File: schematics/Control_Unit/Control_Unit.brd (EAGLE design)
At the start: 58.4 x 86.3 mm, 191 parts, among them IC1 74HC174N, IC10 74HC74N, IC100 74HCT32N, IC101 74HCT08N, IC102 74HC151N, IC103 74HC373N, IC104 74HCT08N, IC105 74HC151N, IC106 74HC151N, IC107 74HCT04N, IC108 74HCT32N, IC109 74HCT08N, IC11 74HC74N, IC110 74HCT32N, IC111 74HC151N, IC112 74HCT32N, IC113 74HC151N, IC114 74HC151N, IC115 74HC151N, IC116 74HC373N, IC117 74HC74N, IC118 74HCT08N, IC119 74HCT08N, IC12 74AC08N, IC120 74HCT04N, IC121 74HCT04N, IC122 74HCT04N, IC123 74HCT04N, IC124 74HCT32N, IC125 74HCT08N, IC126 74AC157N, IC127 74HCT08N, IC128 74AC08N, IC129 74AC08N, IC13 74AC08N, IC130 74HCT04N, IC131 74HCT04N, IC132 74HCT04N, IC133 74HCT04N, IC134 74HCT08N, IC135 74HCT08N, IC136 74HCT08N, IC137 74HCT08N, IC138 74HCT04N, IC139 74HCT08N, IC14 74HC74N, IC140 74HCT08N, IC141 74HCT32N, IC142 74HCT32N, IC143 74HCT32N, IC144 74HCT32N, IC145 74HCT32N, IC146 74HCT32N, IC147 74HCT32N, IC148 74HCT32N, IC15 74HC74N, IC16 74AC08N, IC164 74HC174N, IC165 74HC174N, IC166 74HC174N, IC167 74HC174N, IC168 74HCT32N, IC169 74HCT32N, IC17 74HCT32N, IC172 74HCT32N, IC173 74HCT32N, IC175 74HC193N, IC176 74HC193N, IC177 74HC193N, IC178 74HC193N, IC179 74HC193N, IC18 74AC08N, IC180 74HC193N, IC181 74HC193N, IC182 74HC193N, IC19 74AC08N, IC190 74HCT32N, IC191 74HCT32N, IC2 74HC174N, IC20 74AC08N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

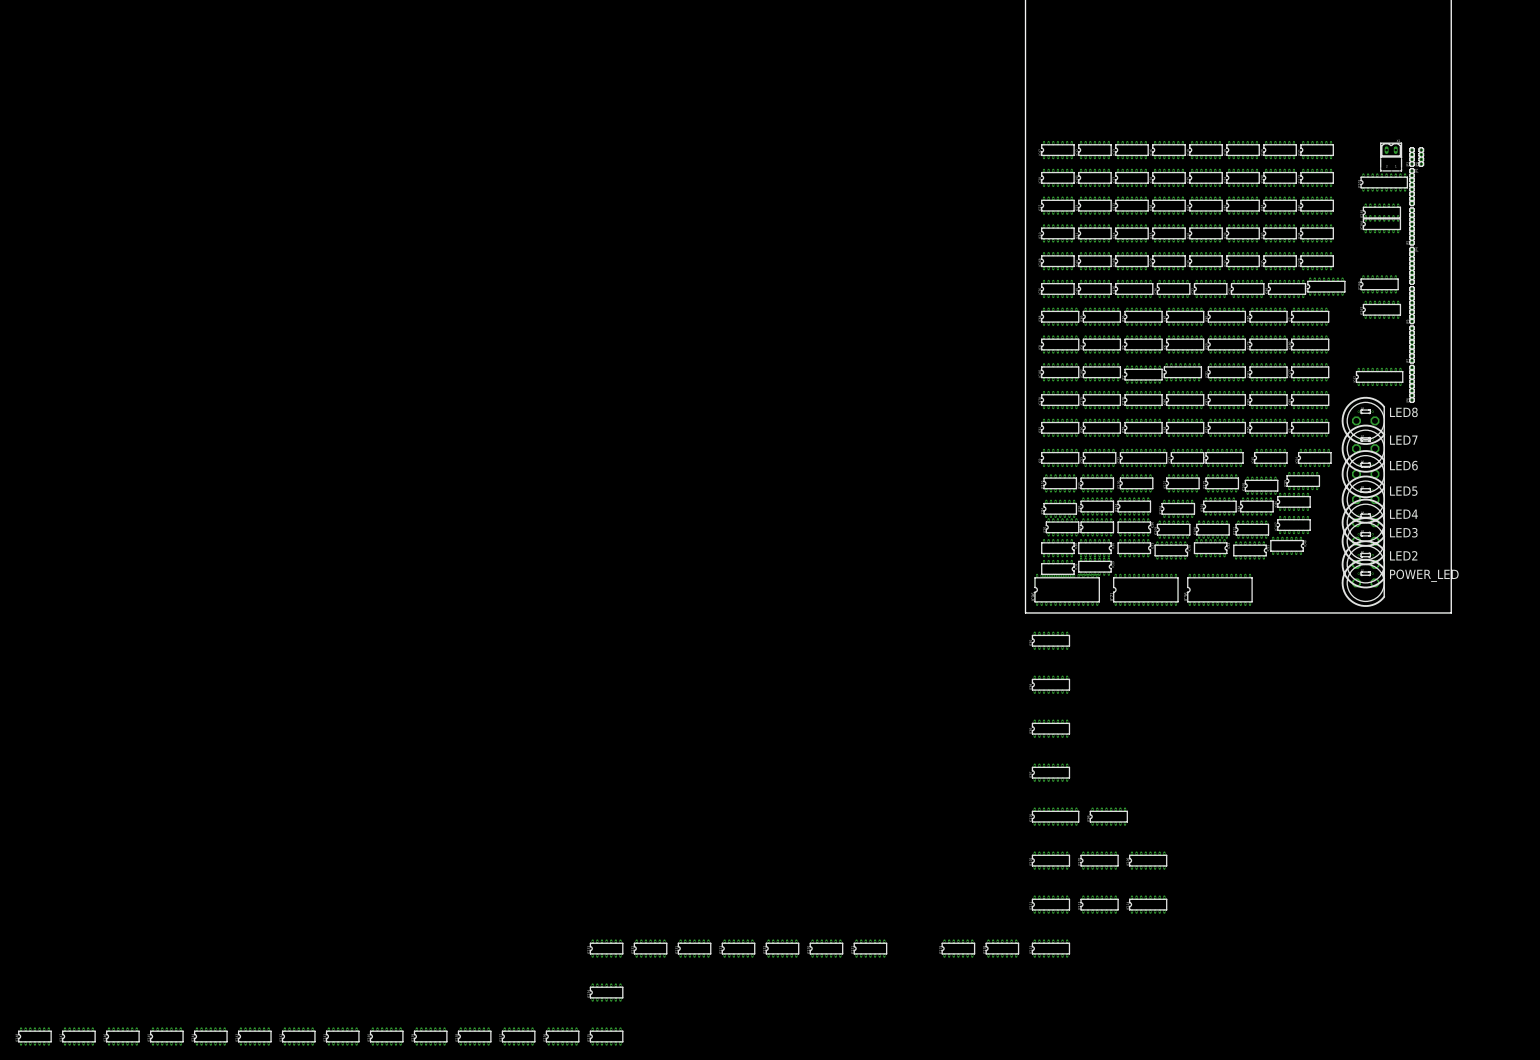
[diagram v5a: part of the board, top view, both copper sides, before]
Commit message: finish ringcounter
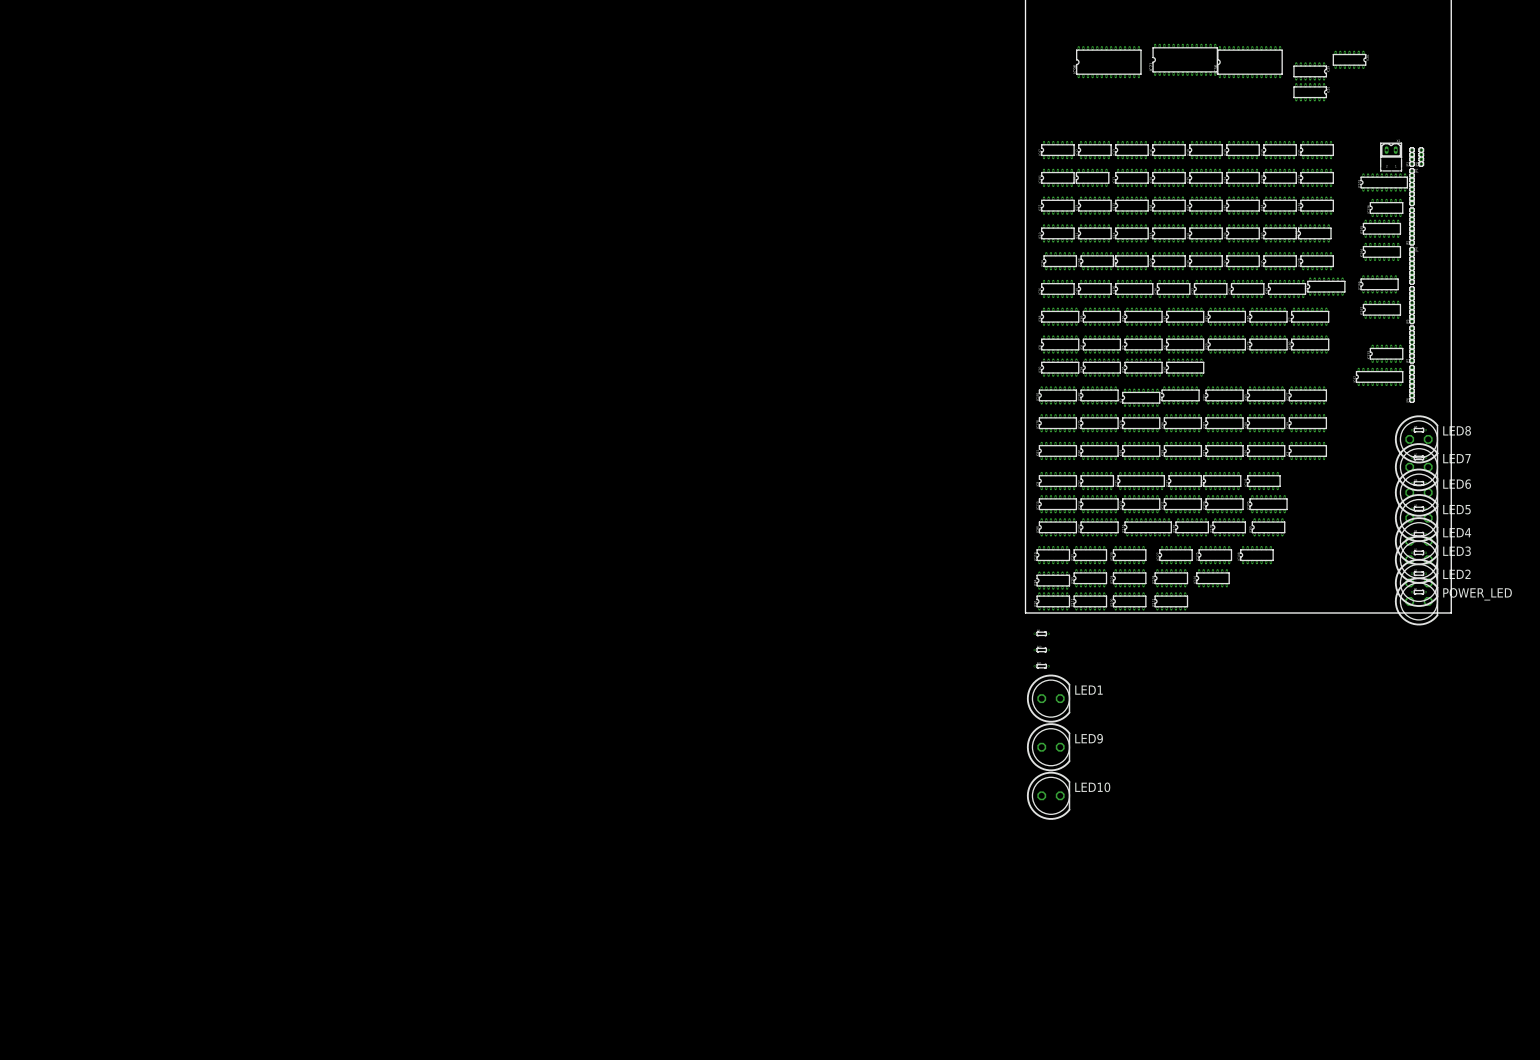
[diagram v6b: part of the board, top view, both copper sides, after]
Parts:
- removed IC118, IC119, IC137, IC139, IC140, IC53, IC64, IC70, IC73, IC90: 74HCT08N, 74xx-eu:DIL14
- removed IC120, IC121, IC122, IC123, IC131, IC132, IC138, IC44, IC45, IC54: 74HCT04N, 74xx-eu:DIL14
- removed IC142, IC143, IC144, IC145, IC146, IC147, IC148, IC31, IC40, IC48, IC85, IC99: 74HCT32N, 74xx-eu:DIL14
- added LED1, LED10, LED9: (no value), led:LED5MM
- added R10, R11, R9: (no value), resistor:0204/7
- moved IC136 160.3 mm to (49.8, 55.6)
- moved IC141 147.6 mm to (33.0, 18.1)
- moved IC135 146.9 mm to (40.0, 52.1)
- moved IC134 145.4 mm to (40.3, 55.9)
- moved IC133 134.6 mm to (49.8, 35.6)
- moved IC81 75.5 mm to (44.8, 75.9)
- moved IC29 74.1 mm to (39.4, 74.3)
- moved IC71 72.9 mm to (22.2, 75.9)
- moved IC96 72.6 mm to (11.7, 75.6)
- moved IC36 72.5 mm to (31.1, 75.6)
- moved IC51 63.4 mm to (39.4, 71.4)
- moved IC115 61.0 mm to (4.76, 14.9)
- moved IC97 58.5 mm to (22.2, 33.7)
- moved IC111 57.8 mm to (21.9, 14.9)
- moved IC114 55.3 mm to (10.5, 14.9)
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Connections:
- net NOT_USED05 renamed NOT_USED5
- net SP_DATA_OUT_15 renamed SP_DATA_OUT_UNUSED
- removed net CARRY_SET_JMPC: IC78.9
- removed net CLR_SP: IC175.14, IC176.14, IC177.14, IC178.14
- removed net CYCL_10: IC10.2, IC117.9
- removed net CYCL_5: IC14.12, IC14.5
- removed net CYCL_6: IC14.9, IC15.2
- removed net CYCL_7: IC15.12, IC15.5
- removed net CYCL_8: IC117.2, IC15.9
- removed net CYCL_9: IC117.12, IC117.5
- removed net DATA10: IC116.6
- removed net DATA11: IC116.9
- removed net DATA12: IC116.12
- removed net DATA13: IC116.15
- removed net DATA14: IC116.16
- removed net DATA15: IC116.19
- removed net DATA8: IC116.2
- removed net DATA9: IC116.5
- removed net RING_CNTR_CLR: IC10.13, IC10.4, IC11.1, IC11.13, IC117.1, IC117.13, IC14.1, IC14.13, IC15.1, IC15.13
- removed net STATE_5: IC101.1, IC127.4
- removed net WRITE_REG_TO_DBUS_JMP_O: IC33.1
- new net !RING_CNTR_RESET: IC10.13, IC10.4, IC11.1, IC11.13, IC117.1, IC117.13, IC14.1, IC14.13, IC15.1, IC15.13, IC43.2
- new net N$225: LED10.A
- new net PC_COUNT_UP_FETCH2: IC124.2, IC14.12, IC14.5
- new net RING_CNTR_RESET: IC43.1
- new net STATE_0: IC101.9, IC14.9, IC15.2, IC23.1, IC23.12, IC24.12, IC27.9, IC28.1, IC38.9, IC51.4, IC74.1, IC74.9, IC78.12, IC81.12
- net ALU_CARRY_OUT: now also IC78.9
- net DATA0: now also IC116.2
- net DATA1: now also IC116.5
- net DATA2: now also IC116.6
- net DATA3: now also IC116.9
- net DATA4: now also IC116.12
- net DATA5: now also IC116.15
- net DATA6: now also IC116.16
- net DATA7: now also IC116.19
- net DATA_BUS_ENABLE_LATCH: now also IC109.3; no longer IC118.11
- net FILL_LR_H_SAVE_LR: now also IC29.9, IC81.3, IC84.12; no longer IC146.4, IC85.1, IC90.6
- net FILL_LR_L_SAVE_LR: now also IC81.8, IC84.9; no longer IC145.4, IC73.3
- net FILL_PC_H_RET: now also IC29.12, IC51.11, IC80.10; no longer IC147.5, IC48.1, IC70.6
- net FILL_PC_L_JMP_O: now also IC84.1; no longer IC148.4
- net FILL_PC_L_RET: now also IC29.4, IC84.2; no longer IC148.5, IC31.1
- net FSDFAFSDFSFDDDDDDDDDDDDDDDDDDDDDDDDDDDDDDDD1: now also IC136.6; no longer IC137.3
- net GND: now also IC102.12, IC102.13, IC102.14, IC102.15, IC105.12, IC105.13, IC105.14, IC105.15, IC106.12, IC106.13, IC106.14, IC106.15, IC111.12, IC111.13, IC111.14, IC111.15, IC113.12, IC113.13, IC113.14, IC113.15, IC114.12, IC114.13, IC114.14, IC114.15, IC115.12, IC115.13, IC115.14, IC115.15, IC98.12, IC98.13, IC98.14, IC98.15, R10.1, R11.1, R9.1; no longer IC1.1, IC118.7, IC119.7, IC120.7, IC121.7, IC122.7, IC123.7, IC131.7, IC132.7, IC137.7, IC138.7, IC139.7, IC140.7, IC142.7, IC143.7, IC144.7, IC145.7, IC146.7, IC147.7, IC148.7, IC179.14, IC180.14, IC181.14, IC182.14, IC2.1, IC2.11, IC2.13, IC2.14, IC2.6, IC31.7, IC4.1, IC40.7, IC44.7, IC45.7, IC48.7, IC5.1, IC5.11, IC5.13, IC5.14, IC5.6, IC50.1, IC50.11, IC50.13, IC50.14, IC50.6, IC53.7, IC54.7, IC6.1, IC62.1, IC64.7, IC65.1, IC65.11, IC65.13, IC65.14, IC65.6, IC66.1, IC67.1, IC67.11, IC67.13, IC67.14, IC67.6, IC68.1, IC69.1, IC69.11, IC69.13, IC69.14, IC69.6, IC7.1, IC70.7, IC73.7, IC8.1, IC8.11, IC8.13, IC8.14, IC8.6, IC82.14, IC83.14, IC85.7, IC90.7, IC92.1, IC94.1, IC94.11, IC94.13, IC94.14, IC94.6, IC95.1, IC97.1, IC97.11, IC97.13, IC97.14, IC97.6, IC99.7
- net INPUT_REG0: now also IC28.4; no longer IC64.9
- net IR_DATA_OUT_7: now also IC125.10; no longer IC125.9
- net LATCH_ALU_INPUT_B_JMP_O: now also IC110.9, IC17.9; no longer IC40.1, IC99.4
- net LATCH_ALU_INPUT_B_PTR_ADD: now also IC110.10; no longer IC99.5
- net LR_H_LOAD_INPUT: now also IC133.13, IC84.11; no longer IC123.3, IC146.6
- net LR_H_LOAD_INPUT_TABLE_1: now also IC84.13; no longer IC146.5
- net LR_L_LOAD_INPUT: now also IC133.11, IC84.8; no longer IC122.3, IC145.6
- net LR_L_LOAD_INPUT_TABLE_1: now also IC84.10; no longer IC145.5
- net N$100: now also IC124.3, IC133.1; no longer IC54.9, IC99.11
- net N$101: now also LED9.K, R10.2; no longer IC110.10
- net N$109: now also IC17.10; no longer IC40.2
- net N$112: now also IC81.11; no longer IC109.3
- net N$115: now also LED1.K, R9.2; no longer IC110.8, IC77.1, IC79.1
- net N$141: now also IC108.11; no longer IC99.3
- net N$142: now also IC108.12; no longer IC99.1
- net N$144: now also IC108.3; no longer IC99.8
- net N$145: now also IC108.2; no longer IC99.10
- net N$152: now also IC110.8; no longer IC99.6
- net N$163: now also IC84.3; no longer IC148.6
- net N$166: now also IC125.9; no longer IC125.10
- net N$167: now also IC133.12; no longer IC123.4
- net N$168: now also LED1.A; no longer IC99.13
- net N$18: now also IC136.5, IC136.9; no longer IC137.2, IC140.1
- net N$194: now also IC81.10, IC81.13, IC81.2; no longer IC109.2, IC73.2, IC90.5
- net N$195: now also LED9.A; no longer IC80.13, IC91.6
- net N$219: now also IC51.10, IC51.13, IC51.5; no longer IC109.5, IC53.5, IC70.5
- net N$22: now also IC28.6; no longer IC64.8
- net N$221: now also IC43.4; no longer IC44.10
- net N$222: now also IC43.6; no longer IC44.12
- net N$223: now also IC29.5, IC51.6; no longer IC109.6, IC31.2
- net N$224: now also IC136.12; no longer IC139.1
- net N$226: now also IC29.13, IC51.8; no longer IC48.2, IC53.6
- net N$233: now also IC29.10; no longer IC85.2
- net N$234: now also IC133.10; no longer IC122.4
- net N$235: now also IC136.11; no longer IC139.3
- net N$239: now also IC136.8; no longer IC140.3
- net N$247: now also IC136.10, IC136.13, IC43.8; no longer IC138.10, IC139.2, IC140.2
- net N$248: now also IC141.9; no longer IC143.1
- net N$249: now also IC141.10, IC141.11; no longer IC142.3, IC143.2
- net N$250: now also IC141.5, IC141.8; no longer IC143.3, IC144.2
- net N$252: now also IC141.6; no longer IC144.3
- net N$266: now also IC109.2, IC109.5; no longer IC118.13, IC119.13
- net N$267: now also IC107.5, IC109.6; no longer IC119.11, IC121.9
- net N$268: now also IC107.12, IC109.1; no longer IC118.12, IC120.8
- net N$269: now also IC107.6; no longer IC121.8
- net N$70: now also IC107.3; no longer IC45.13
- net N$72: now also IC133.6; no longer IC131.6
- net N$73: now also IC133.4; no longer IC132.6
- net N$90: now also IC141.4; no longer IC144.1
- net N$94: now also LED10.K, R11.2; no longer IC164.1, IC165.1, IC165.11, IC165.13, IC165.14, IC165.6, IC166.1, IC167.1, IC167.11, IC167.13, IC167.14, IC167.6
- net N$99: now also IC107.4; no longer IC45.12
- net OPCODE_4: now also IC43.3; no longer IC44.11
- net OPCODE_5: now also IC43.5; no longer IC44.13
- net OPCODE_7: now also IC136.4, IC43.9; no longer IC137.1, IC138.11
- net OUTPUT_REG0_JMP: now also IC28.5; no longer IC64.10
- net PC_COUNT_UP: now also IC133.2; no longer IC54.8
- net PC_COUNT_UP_FETCH1: now also IC124.1, IC80.13, IC91.6; no longer IC99.12
- net PC_HIGH_LOAD_INPUT: now also IC133.3, IC80.8; no longer IC132.5, IC147.6
- net PC_HIGH_LOAD_INPUT_JMP: now also IC80.9; no longer IC147.4
- net PC_H_COUNT_DOWN_JMP_O: now also IC108.1; no longer IC99.9
- net PC_H_COUNT_UP_JMP_O: now also IC108.13; no longer IC99.2
- net PTR_L_LOAD_INPUT: now also IC133.5; no longer IC131.5
- net REGISTER_OUTPUT_SEL_3: now also IC107.13, IC109.4; no longer IC119.12, IC120.9
- net STATE_1: now also IC104.12, IC15.12, IC15.5, IC23.4, IC24.1, IC26.1, IC27.1, IC27.12, IC38.1, IC51.1, IC74.12, IC74.4, IC75.1, IC81.9; no longer IC101.9, IC109.1, IC109.4, IC23.1, IC23.12, IC24.12, IC27.9, IC28.1, IC38.9, IC74.1, IC74.9, IC78.12
- net STATE_2: now also IC104.1, IC117.2, IC15.9, IC23.9, IC24.4, IC26.4, IC27.4, IC28.9, IC38.4, IC51.9, IC75.4, IC81.4; no longer IC104.12, IC23.4, IC24.1, IC26.1, IC27.1, IC27.12, IC38.1, IC51.1, IC73.1, IC74.12, IC74.4, IC75.1
- net STATE_3: now also IC104.9, IC117.12, IC117.5, IC24.9, IC26.9, IC28.12, IC38.12, IC51.12, IC75.12, IC81.1; no longer IC104.1, IC23.9, IC24.4, IC26.4, IC27.4, IC28.9, IC38.4, IC53.4, IC75.4, IC81.4
- net STATE_4: now also IC10.2, IC101.1, IC117.9, IC127.4; no longer IC104.9, IC24.9, IC26.9, IC28.12, IC38.12, IC70.4, IC75.12, IC90.4
- net VCC: now also IC1.1, IC10.1, IC10.10, IC11.10, IC11.4, IC117.10, IC117.4, IC14.10, IC14.4, IC15.10, IC15.4, IC164.1, IC165.1, IC165.11, IC165.13, IC165.14, IC165.6, IC166.1, IC167.1, IC167.11, IC167.13, IC167.14, IC167.6, IC175.14, IC176.14, IC177.14, IC178.14, IC179.14, IC180.14, IC181.14, IC182.14, IC2.1, IC2.11, IC2.13, IC2.14, IC2.6, IC4.1, IC5.1, IC5.11, IC5.13, IC5.14, IC5.6, IC50.1, IC50.11, IC50.13, IC50.14, IC50.6, IC6.1, IC62.1, IC65.1, IC65.11, IC65.13, IC65.14, IC65.6, IC66.1, IC67.1, IC67.11, IC67.13, IC67.14, IC67.6, IC68.1, IC69.1, IC69.11, IC69.13, IC69.14, IC69.6, IC7.1, IC8.1, IC8.11, IC8.13, IC8.14, IC8.6, IC82.14, IC83.14, IC92.1, IC94.1, IC94.11, IC94.13, IC94.14, IC94.6, IC95.1, IC97.1, IC97.11, IC97.13, IC97.14, IC97.6; no longer IC118.14, IC119.14, IC120.14, IC121.14, IC122.14, IC123.14, IC131.14, IC132.14, IC137.14, IC138.14, IC139.14, IC140.14, IC142.14, IC143.14, IC144.14, IC145.14, IC146.14, IC147.14, IC148.14, IC31.14, IC40.14, IC44.14, IC45.14, IC48.14, IC53.14, IC54.14, IC64.14, IC70.14, IC73.14, IC85.14, IC90.14, IC99.14
- net WRITE_LR_H_DBUS_RET: now also IC29.11; no longer IC48.3
- net WRITE_LR_L_DBUS_RET: now also IC29.6; no longer IC31.3
- net WRITE_PC_H_DBUS_SAVE_LR: now also IC141.13, IC29.8; no longer IC142.2, IC85.3
- net WRITE_PC_L_ALU_LATCH_JMP_O: now also IC17.8, IC77.1, IC79.1; no longer IC110.9, IC40.3
- net WRITE_PC_L_DBUS_SAVE_LR: now also IC141.12; no longer IC142.1
- net WRITE_REGB_TO_DBUS_JMP_O: now also IC33.1

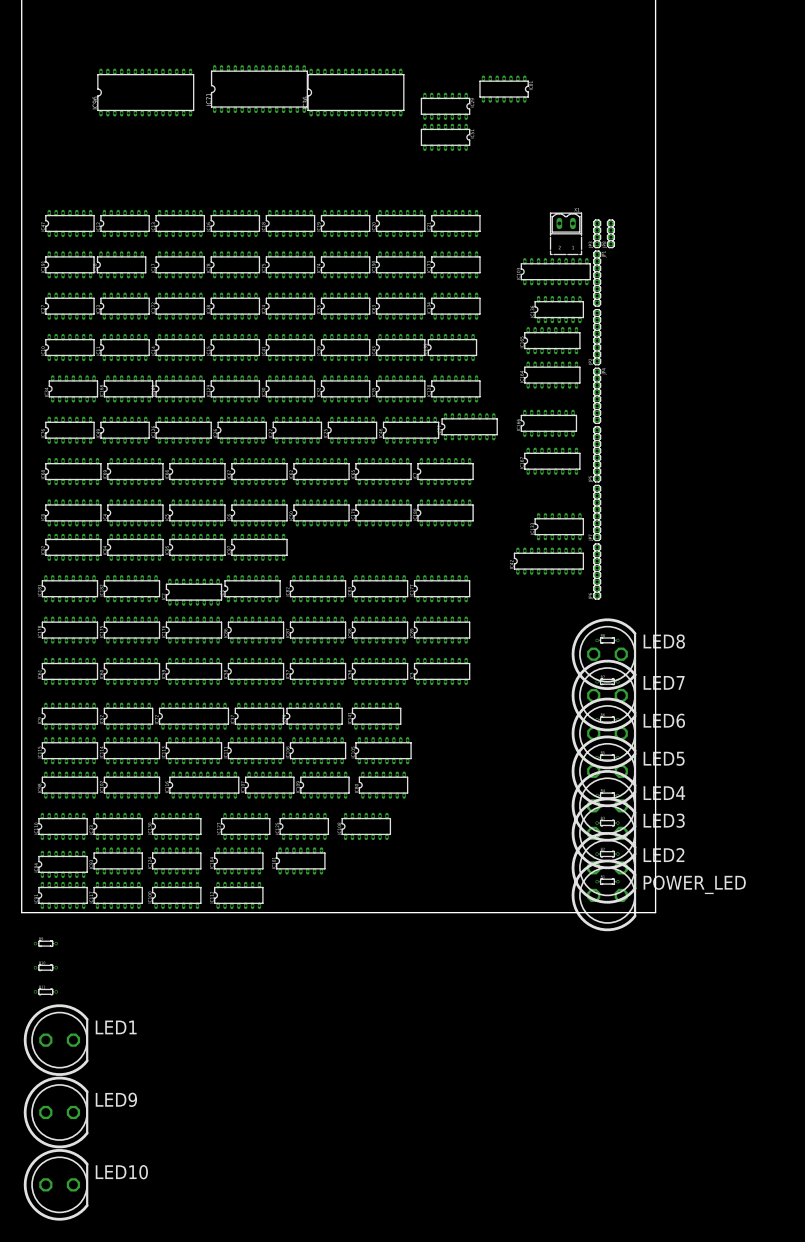
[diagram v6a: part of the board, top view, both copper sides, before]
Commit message: add led library
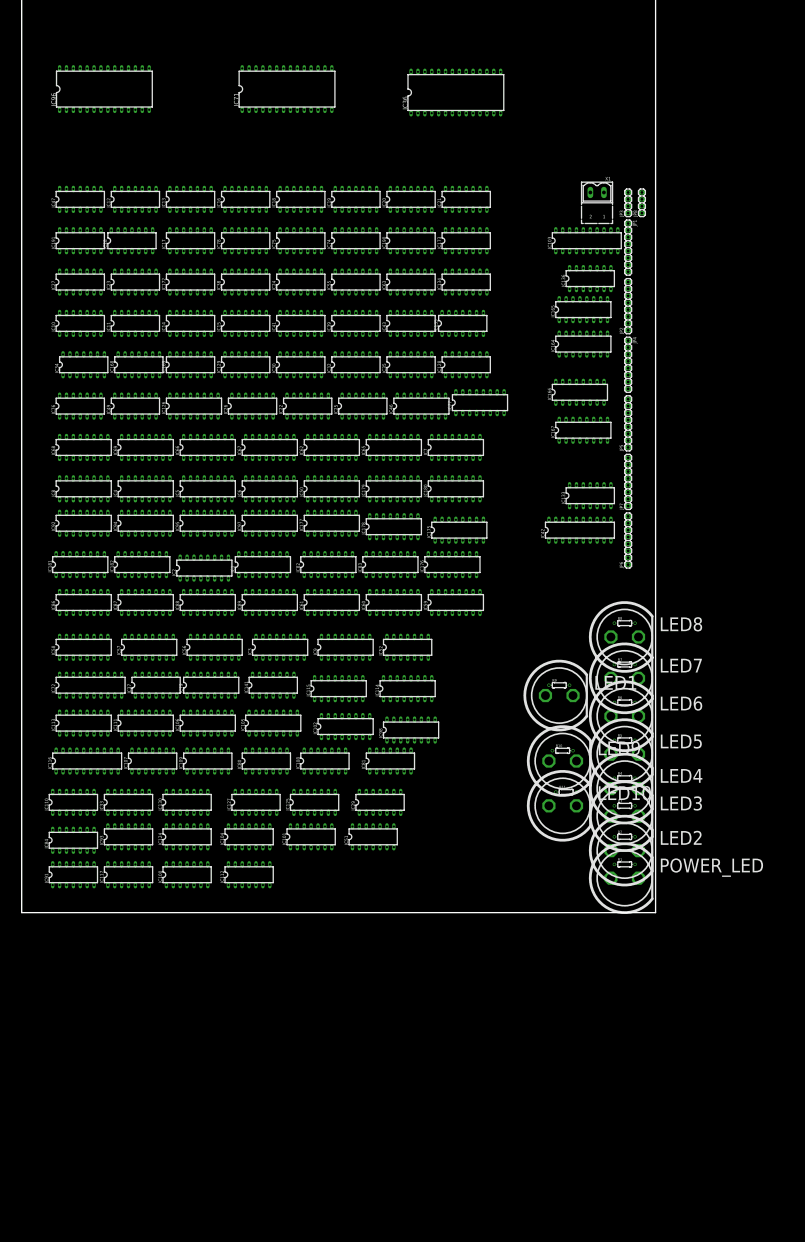
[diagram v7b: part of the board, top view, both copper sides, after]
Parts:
- moved IC51 64.8 mm to (32.7, 6.99), turned to 0 degrees
- moved IC29 64.4 mm to (33.3, 10.2), turned to 0 degrees
- moved IC81 62.8 mm to (34.3, 14.0), turned to 0 degrees
- moved LED10 58.0 mm to (50.2, 9.84)
- moved LED9 56.5 mm to (50.2, 14.0)
- moved LED1 55.9 mm to (49.8, 20.0)
- moved R9 53.0 mm to (49.8, 21.0)
- moved R10 51.7 mm to (50.2, 14.9)
- moved R11 51.4 mm to (50.5, 11.1)
- moved IC98 31.8 mm to (36.2, 16.8)
- moved IC175 31.5 mm to (40.6, 35.2)
- moved IC178 31.3 mm to (34.6, 35.6)
- moved IC52 26.5 mm to (35.9, 24.4)
- moved IC9 26.2 mm to (30.2, 24.4)
- moved IC114 26.0 mm to (35.9, 20.6)
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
